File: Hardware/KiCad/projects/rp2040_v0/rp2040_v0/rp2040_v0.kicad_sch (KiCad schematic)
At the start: 55 parts, among them J1 Conn_01x03, J11 Conn_01x02, J12 Screw_Terminal_01x02, J2 Conn_01x02, J3 Conn_01x03, J4 Conn_01x04, J5 USB_B_Micro, J8 Conn_01x03, J9 Conn_01x02, U1 W25Q128JVSIQTR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

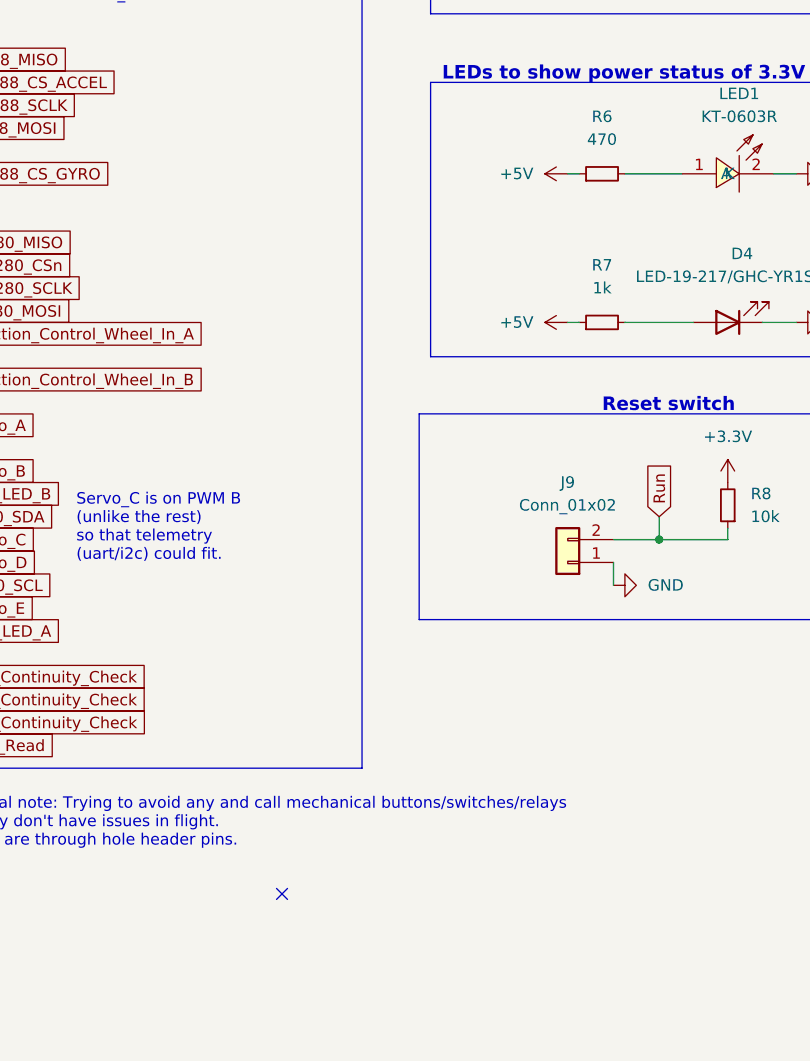
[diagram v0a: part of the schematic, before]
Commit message: Somehow the power rail led indicator got changed to 5v. Change it back
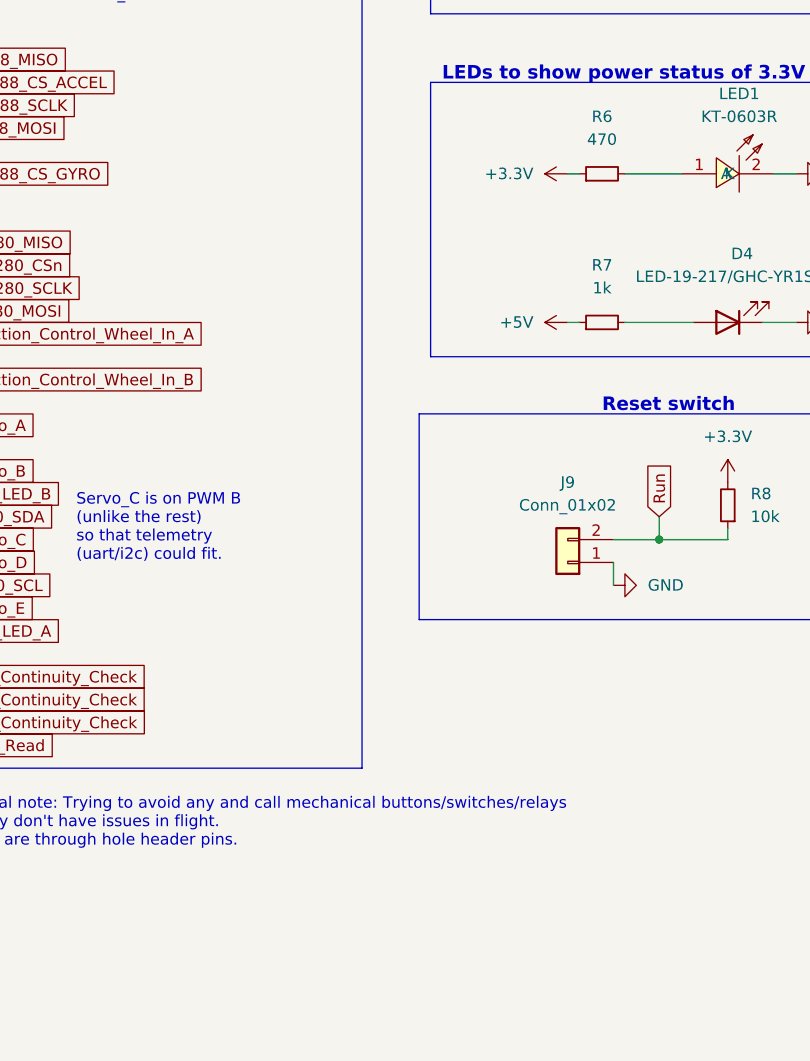
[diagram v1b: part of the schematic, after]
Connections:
- net +3.3V: now also R6.1
- net +5V: no longer R6.1
- no-connect marks 2 -> 1
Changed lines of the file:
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@@
   (junction (at 140.97 64.77) (diameter 0) (color 0 0 0 0)
   )
-  (no_connect (at 215.9 179.07))
   (no_connect (at 132.08 46.99))
   (polyline (pts (xy 284.48 49.53) (xy 254 49.53))
@@
     (pin "1")
   )
-  (symbol (lib_id "power:+5V") (at 247.65 99.06 90) (unit 1)
-    (in_bom yes) (on_board yes) (fields_autoplaced)
-    (property "Reference" "#PWR0101" (id 0) (at 251.46 99.06 0)
-      (effects (font (size 1.27 1.27)) hide)
-    )
-    (property "Value" "+5V" (id 1) (at 243.84 99.0599 90)
-      (effects (font (size 1.27 1.27)) (justify left))
-    )
-    (property "Footprint" "" (id 2) (at 247.65 99.06 0)
-      (effects (font (size 1.27 1.27)) hide)
-    )
-    (property "Datasheet" "" (id 3) (at 247.65 99.06 0)
-      (effects (font (size 1.27 1.27)) hide)
-    )
-    (pin "1")
-  )
   (symbol (lib_id "Connector_Generic:Conn_01x02") (at 247.65 142.24 180) (unit 1)
     (in_bom yes) (on_board yes) (fields_autoplaced)
@@
     (pin "1")
     (pin "2")
+  )
+  (symbol (lib_id "power:+3.3V") (at 247.65 99.06 90) (unit 1)
+    (in_bom yes) (on_board yes) (fields_autoplaced)
+    (property "Reference" "#PWR?" (id 0) (at 251.46 99.06 0)
+      (effects (font (size 1.27 1.27)) hide)
+    )
+    (property "Value" "+3.3V" (id 1) (at 243.84 99.0599 90)
+      (effects (font (size 1.27 1.27)) (justify left))
+    )
+    (property "Footprint" "" (id 2) (at 247.65 99.06 0)
+      (effects (font (size 1.27 1.27)) hide)
+    )
+    (property "Datasheet" "" (id 3) (at 247.65 99.06 0)
+      (effects (font (size 1.27 1.27)) hide)
+    )
+    (pin "1")
   )
   (symbol (lib_id "Regulator_Linear:AMS1117-3.3") (at 74.93 33.02 0) (unit 1)
@@
       (reference "#PWR088") (unit 1) (value "GND") (footprint "")
     )
-    (path "/769b1b53-a834-4720-bd7c-b08ddae529f0"
-      (reference "#PWR0101") (unit 1) (value "+5V") (footprint "")
-    )
     (path "/80e37a29-2645-40c2-ad1a-3b8bdd51b77d/35c70abb-2da0-43a8-af5b-11fc553b71d8"
       (reference "#PWR0102") (unit 1) (value "GND") (footprint "")
@@
       (reference "#PWR0104") (unit 1) (value "+5V") (footprint "")
     )
+    (path "/7aee799c-e7e1-4ec9-b56f-250514197216"
+      (reference "#PWR?") (unit 1) (value "+3.3V") (footprint "")
+    )
     (path "/80e37a29-2645-40c2-ad1a-3b8bdd51b77d/f56621e1-0429-4070-aa37-c7f1ca7e72ef"

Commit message: Remove flash spi testpoints. They're pretty big by default.
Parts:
- removed TP1, TP2, TP3, TP4, TP5, TP6: TestPoint, TestPoint:TestPoint_Pad_1.0x1.0mm, symbol Connector:TestPoint
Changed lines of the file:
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@@
     (pin "2")
-  )
-  (symbol (lib_id "Connector:TestPoint") (at 107.95 109.22 90) (unit 1)
-    (in_bom yes) (on_board yes)
-    (property "Reference" "TP2" (id 0) (at 91.44 109.22 90))
-    (property "Value" "TestPoint" (id 1) (at 99.06 109.22 90))
-    (property "Footprint" "TestPoint:TestPoint_Pad_1.0x1.0mm" (id 2) (at 107.95 104.14 0)
-      (effects (font (size 1.27 1.27)) hide)
-    )
-    (property "Datasheet" "~" (id 3) (at 107.95 104.14 0)
-      (effects (font (size 1.27 1.27)) hide)
-    )
-    (pin "1")
   )
   (symbol (lib_id "Connector:Screw_Terminal_01x02") (at 271.78 25.4 0) (unit 1)
@@
     (pin "3")
   )
-  (symbol (lib_id "Connector:TestPoint") (at 107.95 111.76 90) (unit 1)
-    (in_bom yes) (on_board yes)
-    (property "Reference" "TP3" (id 0) (at 91.44 111.76 90))
-    (property "Value" "TestPoint" (id 1) (at 99.06 111.76 90))
-    (property "Footprint" "TestPoint:TestPoint_Pad_1.0x1.0mm" (id 2) (at 107.95 106.68 0)
-      (effects (font (size 1.27 1.27)) hide)
-    )
-    (property "Datasheet" "~" (id 3) (at 107.95 106.68 0)
-      (effects (font (size 1.27 1.27)) hide)
-    )
-    (pin "1")
-  )
   (symbol (lib_id "power:GND") (at 25.4 106.68 0) (unit 1)
     (in_bom yes) (on_board yes) (fields_autoplaced)
@@
     (pin "2")
   )
-  (symbol (lib_id "Connector:TestPoint") (at 107.95 116.84 90) (unit 1)
-    (in_bom yes) (on_board yes)
-    (property "Reference" "TP5" (id 0) (at 91.44 116.84 90))
-    (property "Value" "TestPoint" (id 1) (at 99.06 116.84 90))
-    (property "Footprint" "TestPoint:TestPoint_Pad_1.0x1.0mm" (id 2) (at 107.95 111.76 0)
-      (effects (font (size 1.27 1.27)) hide)
-    )
-    (property "Datasheet" "~" (id 3) (at 107.95 111.76 0)
-      (effects (font (size 1.27 1.27)) hide)
-    )
-    (pin "1")
-  )
   (symbol (lib_id "power:PWR_FLAG") (at 142.24 24.13 0) (unit 1)
     (in_bom yes) (on_board yes)
@@
     (pin "2")
   )
-  (symbol (lib_id "Connector:TestPoint") (at 107.95 104.14 90) (unit 1)
-    (in_bom yes) (on_board yes)
-    (property "Reference" "TP1" (id 0) (at 91.44 104.14 90))
-    (property "Value" "TestPoint" (id 1) (at 99.06 104.14 90))
-    (property "Footprint" "TestPoint:TestPoint_Pad_1.0x1.0mm" (id 2) (at 107.95 99.06 0)
-      (effects (font (size 1.27 1.27)) hide)
-    )
-    (property "Datasheet" "~" (id 3) (at 107.95 99.06 0)
-      (effects (font (size 1.27 1.27)) hide)
-    )
-    (pin "1")
-  )
   (symbol (lib_id "Regulator_Linear:AMS1117-5.0") (at 157.48 26.67 0) (unit 1)
     (in_bom yes) (on_board yes) (fields_autoplaced)
@@
     (pin "3")
   )
-  (symbol (lib_id "Connector:TestPoint") (at 107.95 114.3 90) (unit 1)
-    (in_bom yes) (on_board yes)
-    (property "Reference" "TP4" (id 0) (at 91.44 114.3 90))
-    (property "Value" "TestPoint" (id 1) (at 99.06 114.3 90))
-    (property "Footprint" "TestPoint:TestPoint_Pad_1.0x1.0mm" (id 2) (at 107.95 109.22 0)
-      (effects (font (size 1.27 1.27)) hide)
-    )
-    (property "Datasheet" "~" (id 3) (at 107.95 109.22 0)
-      (effects (font (size 1.27 1.27)) hide)
-    )
-    (pin "1")
-  )
   (symbol (lib_id "Device:C_Small") (at 87.63 38.1 0) (unit 1)
     (in_bom yes) (on_board yes) (fields_autoplaced)
@@
     )
     (property "Datasheet" "" (id 3) (at 110.49 154.94 0)
-      (effects (font (size 1.27 1.27)) hide)
-    )
-    (pin "1")
-  )
-  (symbol (lib_id "Connector:TestPoint") (at 107.95 119.38 90) (unit 1)
-    (in_bom yes) (on_board yes)
-    (property "Reference" "TP6" (id 0) (at 91.44 119.38 90))
-    (property "Value" "TestPoint" (id 1) (at 99.06 119.38 90))
-    (property "Footprint" "TestPoint:TestPoint_Pad_1.0x1.0mm" (id 2) (at 107.95 114.3 0)
-      (effects (font (size 1.27 1.27)) hide)
-    )
-    (property "Datasheet" "~" (id 3) (at 107.95 114.3 0)
       (effects (font (size 1.27 1.27)) hide)
     )
@@
     )
     (path "/b2681fff-d31e-456f-82ce-345e7022a044/4d94efc3-e1ad-4f1d-acd3-88278ea5b76c"
-      (reference "#PWR?") (unit 1) (value "+5V") (footprint "")
+      (reference "#PWR0105") (unit 1) (value "+5V") (footprint "")
     )
     (path "/80e37a29-2645-40c2-ad1a-3b8bdd51b77d/f56621e1-0429-4070-aa37-c7f1ca7e72ef"
@@
       (reference "R59") (unit 1) (value "470") (footprint "Resistor_SMD:R_0402_1005Metric")
     )
-    (path "/ca4db203-4ae9-4706-a083-67cd713f5b1d"
-      (reference "TP1") (unit 1) (value "TestPoint") (footprint "TestPoint:TestPoint_Pad_1.0x1.0mm")
-    )
-    (path "/433373e8-ca84-46ac-87da-c03703575022"
-      (reference "TP2") (unit 1) (value "TestPoint") (footprint "TestPoint:TestPoint_Pad_1.0x1.0mm")
-    )
-    (path "/5e10b37f-c415-4622-b968-3f665be36998"
-      (reference "TP3") (unit 1) (value "TestPoint") (footprint "TestPoint:TestPoint_Pad_1.0x1.0mm")
-    )
-    (path "/d1bd736a-b4e2-4841-a547-452d3afdb968"
-      (reference "TP4") (unit 1) (value "TestPoint") (footprint "TestPoint:TestPoint_Pad_1.0x1.0mm")
-    )
-    (path "/ae897bb8-e8af-454d-9f78-db2d3cad5c0f"
-      (reference "TP5") (unit 1) (value "TestPoint") (footprint "TestPoint:TestPoint_Pad_1.0x1.0mm")
-    )
-    (path "/e2f63f27-294e-49f0-b6b6-44ea62992862"
-      (reference "TP6") (unit 1) (value "TestPoint") (footprint "TestPoint:TestPoint_Pad_1.0x1.0mm")
-    )
     (path "/3857eacd-a358-4451-8da1-63de73d28dfa"

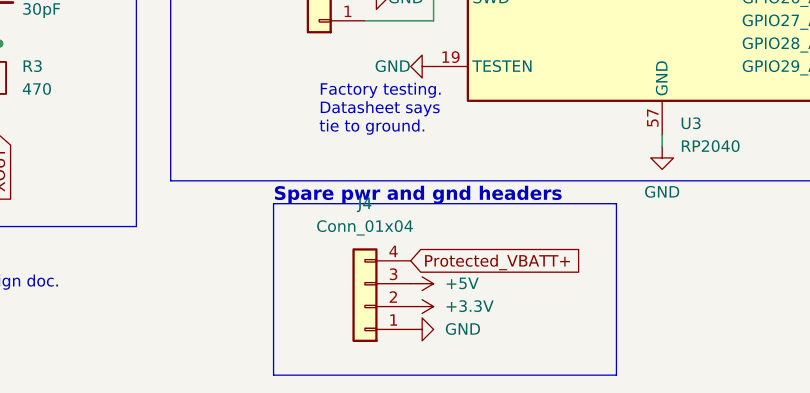
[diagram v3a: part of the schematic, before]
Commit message: put power pins on separate headers so you can't accidently attache a jumper and short things.
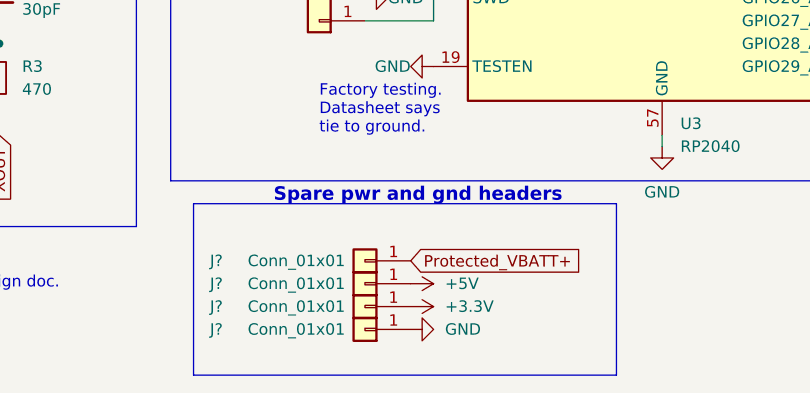
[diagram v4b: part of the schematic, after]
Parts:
- removed J4: Conn_01x04, Connector_PinHeader_2.54mm:PinHeader_1x04_P2.54mm_Vertical, symbol Connector_Generic:Conn_01x04
- added J? (x4): Conn_01x01, Connector_PinHeader_2.54mm:PinHeader_1x01_P2.54mm_Vertical, symbol Connector_Generic:Conn_01x01
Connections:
- net +3.3V: now also J?.1 (Pin_1)
- net +5V: now also J?.1 (Pin_1)
- net -BATT: now also J?.1 (Pin_1)
- net Protected_VBATT+: now also J?.1 (Pin_1)
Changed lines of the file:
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@@
     (stroke (width 0) (type default) (color 0 0 0 0))
   )
-  (polyline (pts (xy 100.33 177.8) (xy 138.43 177.8))
+  (polyline (pts (xy 91.44 177.8) (xy 138.43 177.8))
     (stroke (width 0) (type default) (color 0 0 0 0))
   )
@@
     (stroke (width 0) (type default) (color 0 0 0 0))
   )
-  (polyline (pts (xy 138.43 196.85) (xy 100.33 196.85))
+  (polyline (pts (xy 138.43 196.85) (xy 91.44 196.85))
     (stroke (width 0) (type default) (color 0 0 0 0))
   )
@@
     (stroke (width 0) (type default) (color 0 0 0 0))
   )
-  (polyline (pts (xy 100.33 177.8) (xy 100.33 196.85))
+  (polyline (pts (xy 91.44 177.8) (xy 91.44 196.85))
     (stroke (width 0) (type default) (color 0 0 0 0))
   )
@@
     (pin "3")
   )
+  (symbol (lib_id "Connector_Generic:Conn_01x01") (at 110.49 189.23 180) (unit 1)
+    (in_bom yes) (on_board yes)
+    (property "Reference" "J?" (id 0) (at 93.98 189.23 0))
+    (property "Value" "Conn_01x01" (id 1) (at 102.87 189.23 0))
+    (property "Footprint" "Connector_PinHeader_2.54mm:PinHeader_1x01_P2.54mm_Vertical" (id 2) (at 110.49 189.23 0)
+      (effects (font (size 1.27 1.27)) hide)
+    )
+    (property "Datasheet" "~" (id 3) (at 110.49 189.23 0)
+      (effects (font (size 1.27 1.27)) hide)
+    )
+    (pin "1")
+  )
   (symbol (lib_id "power:GND") (at 25.4 106.68 0) (unit 1)
     (in_bom yes) (on_board yes) (fields_autoplaced)
@@
     (pin "2")
   )
-  (symbol (lib_id "Connector_Generic:Conn_01x04") (at 110.49 189.23 180) (unit 1)
-    (in_bom yes) (on_board yes) (fields_autoplaced)
-    (property "Reference" "J4" (id 0) (at 110.49 177.8 0))
-    (property "Value" "Conn_01x04" (id 1) (at 110.49 180.34 0))
-    (property "Footprint" "Connector_PinHeader_2.54mm:PinHeader_1x04_P2.54mm_Vertical" (id 2) (at 110.49 189.23 0)
-      (effects (font (size 1.27 1.27)) hide)
-    )
-    (property "Datasheet" "~" (id 3) (at 110.49 189.23 0)
-      (effects (font (size 1.27 1.27)) hide)
-    )
-    (pin "1")
-    (pin "2")
-    (pin "3")
-    (pin "4")
-  )
   (symbol (lib_id "Device:C_Small") (at 160.02 68.58 0) (unit 1)
     (in_bom yes) (on_board yes)
@@
     (pin "3")
   )
+  (symbol (lib_id "Connector_Generic:Conn_01x01") (at 110.49 184.15 180) (unit 1)
+    (in_bom yes) (on_board yes)
+    (property "Reference" "J?" (id 0) (at 93.98 184.15 0))
+    (property "Value" "Conn_01x01" (id 1) (at 102.87 184.15 0))
+    (property "Footprint" "Connector_PinHeader_2.54mm:PinHeader_1x01_P2.54mm_Vertical" (id 2) (at 110.49 184.15 0)
+      (effects (font (size 1.27 1.27)) hide)
+    )
+    (property "Datasheet" "~" (id 3) (at 110.49 184.15 0)
+      (effects (font (size 1.27 1.27)) hide)
+    )
+    (pin "1")
+  )
   (symbol (lib_id "Connector_Generic:Conn_01x03") (at 105.41 154.94 180) (unit 1)
     (in_bom yes) (on_board yes) (fields_autoplaced)
@@
     (pin "2")
   )
+  (symbol (lib_id "Connector_Generic:Conn_01x01") (at 110.49 186.69 180) (unit 1)
+    (in_bom yes) (on_board yes)
+    (property "Reference" "J?" (id 0) (at 93.98 186.69 0))
+    (property "Value" "Conn_01x01" (id 1) (at 102.87 186.69 0))
+    (property "Footprint" "Connector_PinHeader_2.54mm:PinHeader_1x01_P2.54mm_Vertical" (id 2) (at 110.49 186.69 0)
+      (effects (font (size 1.27 1.27)) hide)
+    )
+    (property "Datasheet" "~" (id 3) (at 110.49 186.69 0)
+      (effects (font (size 1.27 1.27)) hide)
+    )
+    (pin "1")
+  )
   (symbol (lib_id "power:GND") (at 157.48 36.83 0) (unit 1)
     (in_bom yes) (on_board yes) (fields_autoplaced)
@@
     (pin "1")
     (pin "2")
+  )
+  (symbol (lib_id "Connector_Generic:Conn_01x01") (at 110.49 191.77 180) (unit 1)
+    (in_bom yes) (on_board yes)
+    (property "Reference" "J?" (id 0) (at 93.98 191.77 0))
+    (property "Value" "Conn_01x01" (id 1) (at 102.87 191.77 0))
+    (property "Footprint" "Connector_PinHeader_2.54mm:PinHeader_1x01_P2.54mm_Vertical" (id 2) (at 110.49 191.77 0)
+      (effects (font (size 1.27 1.27)) hide)
+    )
+    (property "Datasheet" "~" (id 3) (at 110.49 191.77 0)
+      (effects (font (size 1.27 1.27)) hide)
+    )
+    (pin "1")
   )
   (symbol (lib_id "power:-BATT") (at 266.7 27.94 90) (unit 1)
@@
       (reference "J3") (unit 1) (value "Conn_01x03") (footprint "Connector_PinHeader_2.54mm:PinHeader_1x03_P2.54mm_Vertical")
     )
-    (path "/7a66bab4-95e4-4c12-9b13-7483eb53e925"
-      (reference "J4") (unit 1) (value "Conn_01x04") (footprint "Connector_PinHeader_2.54mm:PinHeader_1x04_P2.54mm_Vertical")
-    )
     (path "/3362f215-01d0-47bb-95bc-a3a8bc9d2087"
       (reference "J5") (unit 1) (value "USB_B_Micro") (footprint "easyeda2kicad:MICRO-USB-SMD_MICROXNJ")
@@
       (reference "J28") (unit 1) (value "Screw_Terminal_01x02") (footprint "easyeda2kicad:CONN-TH_XY301V-A-5.0-2P")
     )
+    (path "/6137d0ac-1ed4-41ab-b93c-6083d09b10bf"
+      (reference "J?") (unit 1) (value "Conn_01x01") (footprint "Connector_PinHeader_2.54mm:PinHeader_1x01_P2.54mm_Vertical")
+    )
+    (path "/8458783a-0147-49cd-9704-3db5c01e6fe3"
+      (reference "J?") (unit 1) (value "Conn_01x01") (footprint "Connector_PinHeader_2.54mm:PinHeader_1x01_P2.54mm_Vertical")
+    )
+    (path "/b5696ede-8606-4f2d-8627-4db654e29aac"
+      (reference "J?") (unit 1) (value "Conn_01x01") (footprint "Connector_PinHeader_2.54mm:PinHeader_1x01_P2.54mm_Vertical")
+    )
+    (path "/bb4bc4f5-47f9-434a-ac80-d99731d08e26"
+      (reference "J?") (unit 1) (value "Conn_01x01") (footprint "Connector_PinHeader_2.54mm:PinHeader_1x01_P2.54mm_Vertical")
+    )
     (path "/e648d3b1-eed1-4f79-8d45-25203286cbe0"
